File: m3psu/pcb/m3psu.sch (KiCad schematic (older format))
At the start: 6 parts

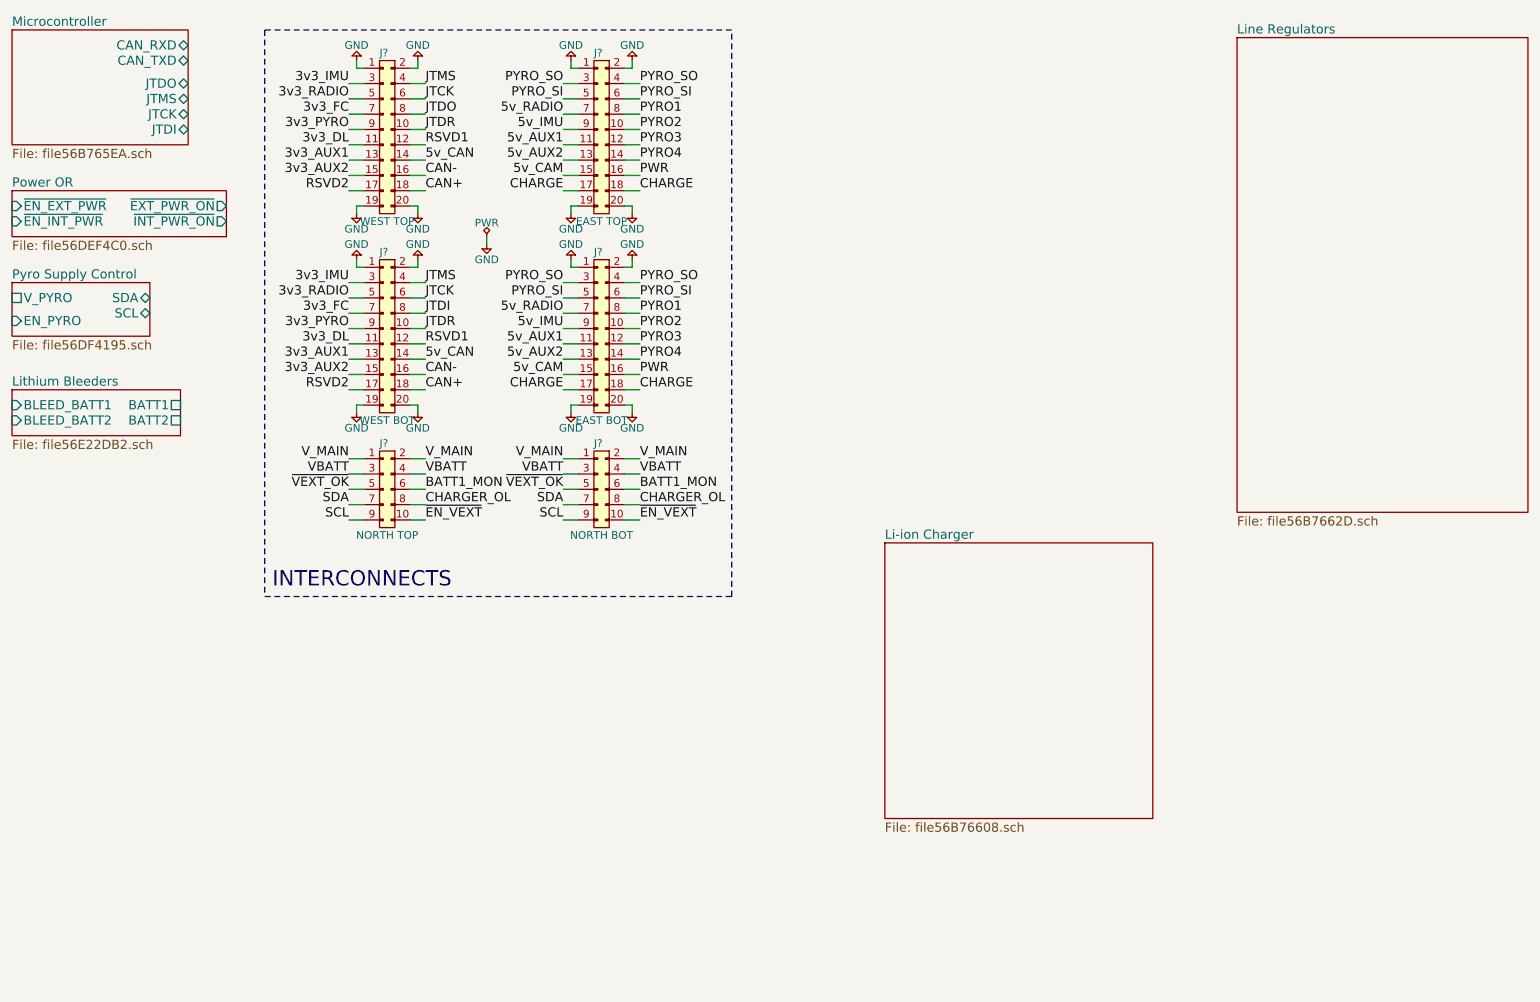
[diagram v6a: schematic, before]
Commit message: Grouped components, sorted internal interconnects. Sheets size now roughly proportional to number of components inside.
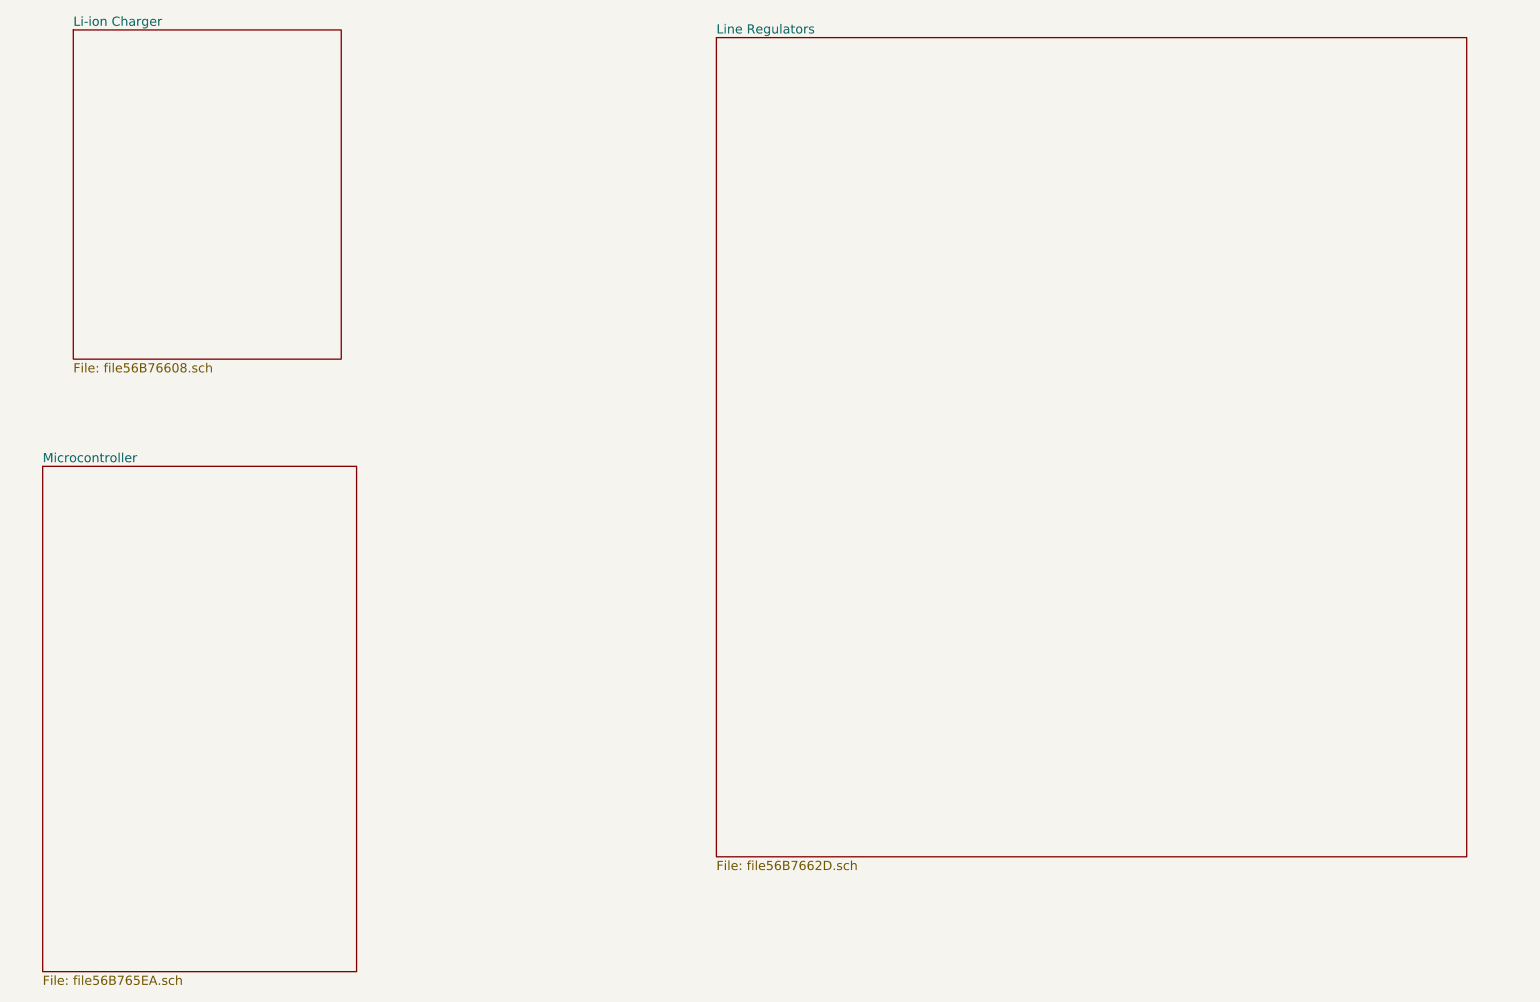
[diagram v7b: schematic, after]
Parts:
- removed J?: WEST TOP, symbol CONN_02x10
- removed J?: EAST TOP, symbol CONN_02x10
- removed J?: WEST BOT, symbol CONN_02x10
- removed J?: EAST BOT, symbol CONN_02x10
- removed J?: NORTH TOP, symbol CONN_02x05
- removed J?: NORTH BOT, symbol CONN_02x05
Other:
- note removed: "INTERCONNECTS"
